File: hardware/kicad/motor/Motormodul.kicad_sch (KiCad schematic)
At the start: 56 parts, among them J100 Stapelstecker links, Pico-Pin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, J101 Kettenstecker, Buchse oben (S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, J102 Kettenstecker, Stift unten (S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, J103 Leistungsstecker, Buchse oben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, J104 Leistungsstecker, Stift unten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, J105 Stapelstecker rechts, Pico-Pi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, J3 Notaus-Ruhestrom, J5 Motor-Klemme, J90 Versorgung Eingang, J95 Randpads GPIO, unbestueckt (T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, J96 Randpads Versorgung: 2x 3V3 +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, Q90 IRFR5305, U1 DRV8876PWPR, U100 STM32C011F6P6, U101 SN74LVC1G175, U102 SN74LVC2G00DCUR, U103 SN74LVC1G08, U3 SN74LVC1G08, U4 PC817, U5 PC817, U6 SN74LVC1G07, U7 SN74LVC1G07, U90 K7805-1000R3

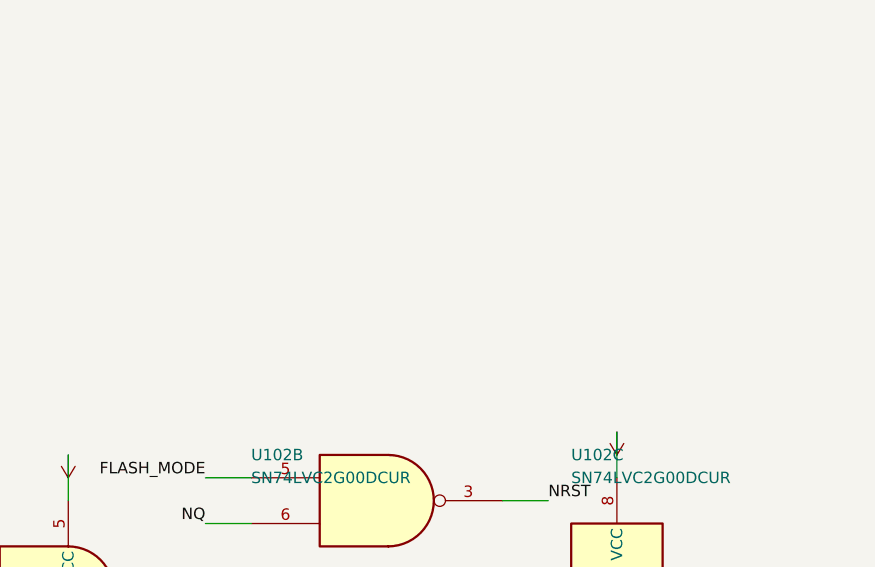
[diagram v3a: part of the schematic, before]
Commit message: Motormodul: fehlende Gatter-Abblockung fuer U101/U102/U103 nachgezogen
Dieselbe Luecke, die Task 6 im Dimmermodul geschlossen hat, bestand im
Motormodul unveraendert: modulsockel.py blockt mit C100 nur die MCU
(U100) ab, C101 ist Teil des NCLR-Loeschglieds -- U101 (SN74LVC1G175),
U102 (SN74LVC2G00DCUR) und U103 (SN74LVC1G08) hatten keinen eigenen
100-nF-Kondensator an ihrer 3V3/GND-Versorgung. Die EIGENEN Gatter des
Motormoduls (U3/U6/U7) waren davon nicht betroffen -- die haben schon
laenger ihre eigenen Abblockkondensatoren C14/C15/C16.

Neue Funktion _gatter_abblockung_sockel() in tools/sch/motormodul.py
setzt C17/C18/C19 (100n/0805, LCSC C49678) an dieselben x/y-Offsets,
die dimmermodul.py fuer C102/C103/C104 verwendet, weil der
Modulsockel-Block in beiden Modulen identischer Code ist. ERC bleibt
bei 0 Fehlern und den zwei vorbestehenden Warnungen
(lib_symbol_mismatch, multiple_net_names). tests/test_motormodul.py
um die drei neuen Refs und eine Gattungspruefung (Pin1->3V3,
Pin2->GND) erweitert.

Co-Authored-By: Claude Fable 5 <noreply@anthropic.com>
Claude-Session: https://claude.ai/code/session_01KDus95JJwCeRuwccgBWEi5
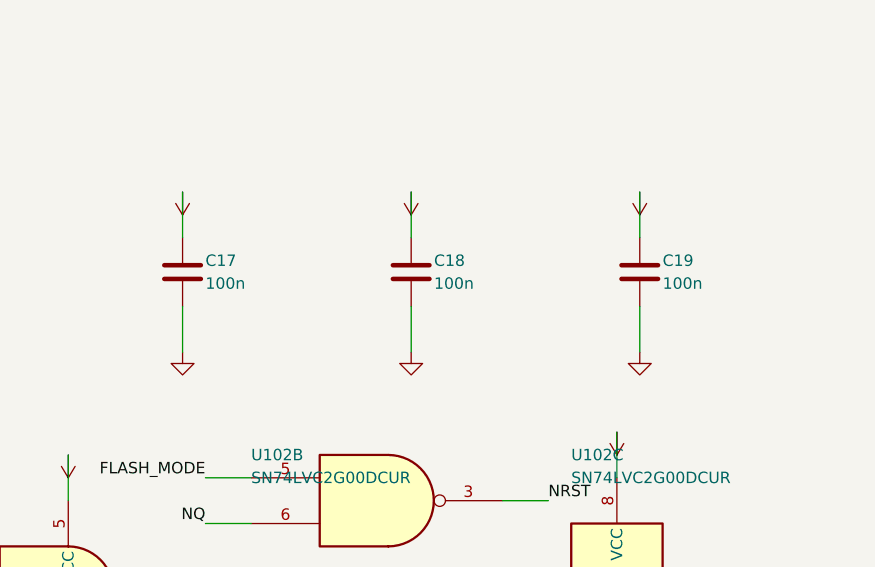
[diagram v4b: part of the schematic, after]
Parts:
- removed C91: 22u, Capacitor_SMD:C_0805_2012Metric_Pad1.18x1.45mm_HandSolder, symbol Device:C
- removed J100: Stapelstecker links, Pico-Pins 1..20 (Buchse), Connector_PinSocket_2.54mm:PinSocket_1x20_P2.54mm_Vertical, symbol Connector_Generic:Conn_01x20
- removed J101: Kettenstecker, Buchse oben (SMD), Connector_PinSocket_2.54mm:PinSocket_1x02_P2.54mm_Vertical_SMD_Pin1Left, symbol Connector_Generic:Conn_01x02
- removed J102: Kettenstecker, Stift unten (SMD), Connector_PinHeader_2.54mm:PinHeader_1x02_P2.54mm_Vertical_SMD_Pin1Left, symbol Connector_Generic:Conn_01x02
- removed J103: Leistungsstecker, Buchse oben (SMD), Connector_PinSocket_2.54mm:PinSocket_2x02_P2.54mm_Vertical_SMD, symbol Connector_Generic:Conn_02x02_Odd_Even
- removed J104: Leistungsstecker, Stift unten (SMD), Connector_PinHeader_2.54mm:PinHeader_2x02_P2.54mm_Vertical_SMD, symbol Connector_Generic:Conn_02x02_Odd_Even
- removed J105: Stapelstecker rechts, Pico-Pins 21..40 (Buchse), Connector_PinSocket_2.54mm:PinSocket_1x20_P2.54mm_Vertical, symbol Connector_Generic:Conn_01x20
- removed U1: DRV8876PWPR, DRV8876PWPR:IC_DRV8876PWPR, symbol DRV8876PWPR:DRV8876PWPR
- removed U90: K7805-1000R3, Converter_DCDC:Converter_DCDC_RECOM_R-78B-2.0_THT, symbol Converter_DCDC:R-78B5.0-2.0
- added C15, C16: 0.1u, Capacitor_SMD:C_0805_2012Metric_Pad1.18x1.45mm_HandSolder, symbol Device:C
- added R100, R101: Kennwiderstand (Modultyp), Resistor_SMD:R_0805_2012Metric_Pad1.20x1.40mm_HandSolder, symbol Device:R
- added R104: 10000 (ID_OBEN), Resistor_SMD:R_0805_2012Metric_Pad1.20x1.40mm_HandSolder, symbol Device:R
- added R17, R19: 3.3k, Resistor_SMD:R_1206_3216Metric, symbol Device:R
- added R20, R21: 4.7k, Resistor_SMD:R_0805_2012Metric_Pad1.20x1.40mm_HandSolder, symbol Device:R
- added U5: PC817, Optocoupler_PC817:PC817_SMT_Gullwing, symbol Isolator:PC817
- added U6, U7: SN74LVC1G07, Package_TO_SOT_SMD:SOT-353_SC-70-5, symbol 74xGxx:74LVC1G07
- C10: renamed from J5; value Motor-Klemme -> 0.022u; footprint TerminalBlock_Phoenix:TerminalBlock_Phoenix_MKDS-3-2-5.08_1x02_P5.08mm_Horizontal -> Capacitor_SMD:C_0805_2012Metric_Pad1.18x1.45mm_HandSolder; symbol Connector:Screw_Terminal_01x02 -> Device:C
- C100: renamed from U102; value SN74LVC2G00DCUR -> 100n; footprint Package_SO:VSSOP-8_2.3x2mm_P0.5mm -> Capacitor_SMD:C_0805_2012Metric_Pad1.18x1.45mm_HandSolder; symbol 74xGxx:74LVC2G00 -> Device:C
- C101: renamed from R100; value Kennwiderstand (Modultyp) -> 1000n; footprint Resistor_SMD:R_0805_2012Metric_Pad1.20x1.40mm_HandSolder -> Capacitor_SMD:C_0805_2012Metric_Pad1.18x1.45mm_HandSolder; symbol Device:R -> Device:C
- C11: renamed from U3; value SN74LVC1G08 -> 0.1u; footprint Package_TO_SOT_SMD:SOT-353_SC-70-5 -> Capacitor_SMD:C_0805_2012Metric_Pad1.18x1.45mm_HandSolder; symbol 74xGxx:74LVC1G08 -> Device:C
- C13: renamed from R20; value 4.7k -> 0.1u; footprint Resistor_SMD:R_0805_2012Metric_Pad1.20x1.40mm_HandSolder -> Capacitor_SMD:C_0805_2012Metric_Pad1.18x1.45mm_HandSolder; symbol Device:R -> Device:C
- C14: renamed from R17; value 3.3k -> 0.1u; footprint Resistor_SMD:R_1206_3216Metric -> Capacitor_SMD:C_0805_2012Metric_Pad1.18x1.45mm_HandSolder; symbol Device:R -> Device:C
- C17: renamed from R91; value 10k -> 100n; footprint Resistor_SMD:R_0805_2012Metric_Pad1.20x1.40mm_HandSolder -> Capacitor_SMD:C_0805_2012Metric_Pad1.18x1.45mm_HandSolder; symbol Device:R -> Device:C; LCSC (none) -> C49678
- C18: renamed from D90; value SMCJ30A -> 100n; footprint Diode_SMD:D_SMC -> Capacitor_SMD:C_0805_2012Metric_Pad1.18x1.45mm_HandSolder; symbol Device:D_Zener -> Device:C; LCSC (none) -> C49678
- C19: renamed from C90; value 220u -> 100n; footprint Capacitor_THT:CP_Radial_D8.0mm_P3.50mm -> Capacitor_SMD:C_0805_2012Metric_Pad1.18x1.45mm_HandSolder; symbol Device:C_Polarized -> Device:C; LCSC (none) -> C49678
- C90: renamed from R8; value 0.1k -> 220u; footprint Resistor_SMD:R_0805_2012Metric_Pad1.20x1.40mm_HandSolder -> Capacitor_THT:CP_Radial_D8.0mm_P3.50mm; symbol Device:R -> Device:C_Polarized
- C91: renamed from R13; value 10k -> 22u; footprint Resistor_SMD:R_0805_2012Metric_Pad1.20x1.40mm_HandSolder -> Capacitor_SMD:C_0805_2012Metric_Pad1.18x1.45mm_HandSolder; symbol Device:R -> Device:C
- D90: renamed from R7; value 0.1k -> SMCJ30A; footprint Resistor_SMD:R_0805_2012Metric_Pad1.20x1.40mm_HandSolder -> Diode_SMD:D_SMC; symbol Device:R -> Device:D_Zener
- D91: renamed from R5; value 1.3k -> SS36C; footprint Resistor_SMD:R_0805_2012Metric_Pad1.20x1.40mm_HandSolder -> Diode_SMD:D_SMC; symbol Device:R -> Device:D_Schottky
- J100: renamed from U100; value STM32C011F6P6 -> Stapelstecker links, Pico-Pins 1..20 (Buchse); footprint Package_SO:TSSOP-20_4.4x6.5mm_P0.65mm -> Connector_PinSocket_2.54mm:PinSocket_1x20_P2.54mm_Vertical; symbol MCU_ST_STM32C0:STM32C011F6Px -> Connector_Generic:Conn_01x20
- J101: renamed from U101; value SN74LVC1G175 -> Kettenstecker, Buchse oben (SMD); footprint Package_TO_SOT_SMD:SOT-363_SC-70-6 -> Connector_PinSocket_2.54mm:PinSocket_1x02_P2.54mm_Vertical_SMD_Pin1Left; symbol 74xGxx:74LVC1G175 -> Connector_Generic:Conn_01x02
- J102: renamed from R102; value 100k -> Kettenstecker, Stift unten (SMD); footprint Resistor_SMD:R_0805_2012Metric_Pad1.20x1.40mm_HandSolder -> Connector_PinHeader_2.54mm:PinHeader_1x02_P2.54mm_Vertical_SMD_Pin1Left; symbol Device:R -> Connector_Generic:Conn_01x02
- J103: renamed from C101; value 1000n -> Leistungsstecker, Buchse oben (SMD); footprint Capacitor_SMD:C_0805_2012Metric_Pad1.18x1.45mm_HandSolder -> Connector_PinSocket_2.54mm:PinSocket_2x02_P2.54mm_Vertical_SMD; symbol Device:C -> Connector_Generic:Conn_02x02_Odd_Even
- J104: renamed from U102; value SN74LVC2G00DCUR -> Leistungsstecker, Stift unten (SMD); footprint Package_SO:VSSOP-8_2.3x2mm_P0.5mm -> Connector_PinHeader_2.54mm:PinHeader_2x02_P2.54mm_Vertical_SMD; symbol 74xGxx:74LVC2G00 -> Connector_Generic:Conn_02x02_Odd_Even
- J105: renamed from C100; value 100n -> Stapelstecker rechts, Pico-Pins 21..40 (Buchse); footprint Capacitor_SMD:C_0805_2012Metric_Pad1.18x1.45mm_HandSolder -> Connector_PinSocket_2.54mm:PinSocket_1x20_P2.54mm_Vertical; symbol Device:C -> Connector_Generic:Conn_01x20
- J3: renamed from U5; value PC817 -> Notaus-Ruhestrom; footprint Optocoupler_PC817:PC817_SMT_Gullwing -> Connector_PinHeader_2.54mm:PinHeader_1x04_P2.54mm_Vertical; symbol Isolator:PC817 -> Connector:Conn_01x04_Pin
- J5: renamed from U6; value SN74LVC1G07 -> Motor-Klemme; footprint Package_TO_SOT_SMD:SOT-353_SC-70-5 -> TerminalBlock_Phoenix:TerminalBlock_Phoenix_MKDS-3-2-5.08_1x02_P5.08mm_Horizontal; symbol 74xGxx:74LVC1G07 -> Connector:Screw_Terminal_01x02; LCSC C7830 -> (none)
- J90: renamed from D91; value SS36C -> Versorgung Eingang; footprint Diode_SMD:D_SMC -> TerminalBlock_Phoenix:TerminalBlock_Phoenix_PT-1,5-2-3.5-H_1x02_P3.50mm_Horizontal; symbol Device:D_Schottky -> Connector:Screw_Terminal_01x02
- J95: renamed from Q90; value IRFR5305 -> Randpads GPIO, unbestueckt (THT-Loetpad); footprint Package_TO_SOT_SMD:TO-252-3_TabPin2 -> Connector_PinHeader_2.54mm:PinHeader_1x18_P2.54mm_Vertical; symbol Transistor_FET:Q_PMOS_GDS -> Connector_Generic:Conn_01x18; now not fitted
- J96: renamed from R90; value 10k -> Randpads Versorgung: 2x 3V3 + 2x GND, unbestueckt (THT-Loetpad); footprint Resistor_SMD:R_0805_2012Metric_Pad1.20x1.40mm_HandSolder -> Connector_PinHeader_2.54mm:PinHeader_1x04_P2.54mm_Vertical; symbol Device:R -> Connector_Generic:Conn_01x04; now not fitted
- Q90: renamed from C9; value 0.1u -> IRFR5305; footprint Capacitor_SMD:C_0805_2012Metric_Pad1.18x1.45mm_HandSolder -> Package_TO_SOT_SMD:TO-252-3_TabPin2; symbol Device:C -> Transistor_FET:Q_PMOS_GDS
- R10: renamed from U4; value PC817 -> 4.7k; footprint Optocoupler_PC817:PC817_SMT_Gullwing -> Resistor_SMD:R_0805_2012Metric_Pad1.20x1.40mm_HandSolder; symbol Isolator:PC817 -> Device:R; now not fitted
- R102: renamed from R104; value 10000 (ID_OBEN) -> 100k
- R105: renamed from J90; value Versorgung Eingang -> 10000 (ID_OBEN); footprint TerminalBlock_Phoenix:TerminalBlock_Phoenix_PT-1,5-2-3.5-H_1x02_P3.50mm_Horizontal -> Resistor_SMD:R_0805_2012Metric_Pad1.20x1.40mm_HandSolder; symbol Connector:Screw_Terminal_01x02 -> Device:R
- R13: renamed from R16; value 3.3k -> 10k; footprint Resistor_SMD:R_1206_3216Metric -> Resistor_SMD:R_0805_2012Metric_Pad1.20x1.40mm_HandSolder
- R15: renamed from R19; value 3.3k -> 10k; footprint Resistor_SMD:R_1206_3216Metric -> Resistor_SMD:R_0805_2012Metric_Pad1.20x1.40mm_HandSolder
- R16: renamed from R21; value 4.7k -> 3.3k; footprint Resistor_SMD:R_0805_2012Metric_Pad1.20x1.40mm_HandSolder -> Resistor_SMD:R_1206_3216Metric
- R18: renamed from U7; value SN74LVC1G07 -> 3.3k; footprint Package_TO_SOT_SMD:SOT-353_SC-70-5 -> Resistor_SMD:R_1206_3216Metric; symbol 74xGxx:74LVC1G07 -> Device:R; LCSC C7830 -> (none)
- R5: renamed from R18; value 3.3k -> 1.3k; footprint Resistor_SMD:R_1206_3216Metric -> Resistor_SMD:R_0805_2012Metric_Pad1.20x1.40mm_HandSolder
- R7: renamed from C14; value 0.1u -> 0.1k; footprint Capacitor_SMD:C_0805_2012Metric_Pad1.18x1.45mm_HandSolder -> Resistor_SMD:R_0805_2012Metric_Pad1.20x1.40mm_HandSolder; symbol Device:C -> Device:R
- R8: renamed from R15; value 10k -> 0.1k
- R9: renamed from J3; value Notaus-Ruhestrom -> 0.1k; footprint Connector_PinHeader_2.54mm:PinHeader_1x04_P2.54mm_Vertical -> Resistor_SMD:R_0805_2012Metric_Pad1.20x1.40mm_HandSolder; symbol Connector:Conn_01x04_Pin -> Device:R
- R90: renamed from C10; value 0.022u -> 10k; footprint Capacitor_SMD:C_0805_2012Metric_Pad1.18x1.45mm_HandSolder -> Resistor_SMD:R_0805_2012Metric_Pad1.20x1.40mm_HandSolder; symbol Device:C -> Device:R
- R91: renamed from C11; value 0.1u -> 10k; footprint Capacitor_SMD:C_0805_2012Metric_Pad1.18x1.45mm_HandSolder -> Resistor_SMD:R_0805_2012Metric_Pad1.20x1.40mm_HandSolder; symbol Device:C -> Device:R
- U1: renamed from R10; value 4.7k -> DRV8876PWPR; footprint Resistor_SMD:R_0805_2012Metric_Pad1.20x1.40mm_HandSolder -> DRV8876PWPR:IC_DRV8876PWPR; symbol Device:R -> DRV8876PWPR:DRV8876PWPR; now fitted
- U100: renamed from U102; value SN74LVC2G00DCUR -> STM32C011F6P6; footprint Package_SO:VSSOP-8_2.3x2mm_P0.5mm -> Package_SO:TSSOP-20_4.4x6.5mm_P0.65mm; symbol 74xGxx:74LVC2G00 -> MCU_ST_STM32C0:STM32C011F6Px
- U101: renamed from U103; value SN74LVC1G08 -> SN74LVC1G175; footprint Package_TO_SOT_SMD:SOT-353_SC-70-5 -> Package_TO_SOT_SMD:SOT-363_SC-70-6; symbol 74xGxx:74LVC1G08 -> 74xGxx:74LVC1G175
- U102: renamed from J95; value Randpads GPIO, unbestueckt (THT-Loetpad) -> SN74LVC2G00DCUR; footprint Connector_PinHeader_2.54mm:PinHeader_1x18_P2.54mm_Vertical -> Package_SO:VSSOP-8_2.3x2mm_P0.5mm; symbol Connector_Generic:Conn_01x18 -> 74xGxx:74LVC2G00; now fitted
- U102: renamed from R105; value 10000 (ID_OBEN) -> SN74LVC2G00DCUR; footprint Resistor_SMD:R_0805_2012Metric_Pad1.20x1.40mm_HandSolder -> Package_SO:VSSOP-8_2.3x2mm_P0.5mm; symbol Device:R -> 74xGxx:74LVC2G00
- U102: renamed from R101; value Kennwiderstand (Modultyp) -> SN74LVC2G00DCUR; footprint Resistor_SMD:R_0805_2012Metric_Pad1.20x1.40mm_HandSolder -> Package_SO:VSSOP-8_2.3x2mm_P0.5mm; symbol Device:R -> 74xGxx:74LVC2G00
- U103: renamed from J96; value Randpads Versorgung: 2x 3V3 + 2x GND, unbestueckt (THT-Loetpad) -> SN74LVC1G08; footprint Connector_PinHeader_2.54mm:PinHeader_1x04_P2.54mm_Vertical -> Package_TO_SOT_SMD:SOT-353_SC-70-5; symbol Connector_Generic:Conn_01x04 -> 74xGxx:74LVC1G08; now fitted
- U3: renamed from C15; value 0.1u -> SN74LVC1G08; footprint Capacitor_SMD:C_0805_2012Metric_Pad1.18x1.45mm_HandSolder -> Package_TO_SOT_SMD:SOT-353_SC-70-5; symbol Device:C -> 74xGxx:74LVC1G08
- U4: renamed from C16; value 0.1u -> PC817; footprint Capacitor_SMD:C_0805_2012Metric_Pad1.18x1.45mm_HandSolder -> Optocoupler_PC817:PC817_SMT_Gullwing; symbol Device:C -> Isolator:PC817
- U90: renamed from R9; value 0.1k -> K7805-1000R3; footprint Resistor_SMD:R_0805_2012Metric_Pad1.20x1.40mm_HandSolder -> Converter_DCDC:Converter_DCDC_RECOM_R-78B-2.0_THT; symbol Device:R -> Converter_DCDC:R-78B5.0-2.0
- renumbered C13 to C9
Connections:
- net +24V: now also C11.2, C9.1, C90.1, D90.1 (K), J103.1 (Pin_1), J103.3 (Pin_3), J104.1 (Pin_1), J104.3 (Pin_3), Q90.3 (S), R16.1, R90.2, U1.11 (VM), U90.1 (IN), R17.1; no longer C14.1, C18.1 (K), C19.1, J95.3 (S), J96.2, Q90.1, R13.1, R91.2
- net +5V_LOKAL: now also C91.1, D91.2 (A), U90.3 (OUT); no longer J90.2 (A)
- net 3V3: now also C100.1, C100.2, C11.1, C14.1, C14.2, C17.1, C18.1, C19.1, C90.2, C91.2, D90.2 (A), J100.13 (Pin_13), J100.18 (Pin_18), J100.3 (Pin_3), J100.8 (Pin_8), J102.2 (Pin_2), J103.4 (Pin_4), J104.2 (Pin_2), J104.4 (Pin_4), J105.13 (Pin_13), J105.16 (Pin_16), J105.18 (Pin_18), J105.3 (Pin_3), J105.8 (Pin_8), J90.2 (Pin_2), J96.1 (Pin_1), J96.2 (Pin_2), J96.3 (Pin_3), J96.4 (Pin_4), R105.1, R13.1, R15.1, R5.2, R91.2, U1.15 (GND), U1.16 (PMODE), U1.17 (EXP), U1.5 (VREF), U1.7 (IMODE), U1.9 (PGND), U100.4 (VDD), U100.5 (VSS), U101.2 (GND), U102.4 (GND), U102.8 (VCC), U103.5 (VCC), U3.3 (GND), U3.5 (VCC), U4.4, U90.2 (GND), C15.1, C15.2, C16.1, C16.2, R100.2, R101.2, R104.1, R20.2, R21.2, U5.2, U5.4, U6.3 (GND), U6.5 (VCC), U7.3 (GND), U7.5 (VCC); no longer C100.4 (GND), C100.8 (VCC), C11.3 (GND), C11.5 (VCC), C9.2, C91.1, D91.2, J100.4 (VDD), J100.5 (VSS), J101.5 (VCC), J102.1, J105.1, J105.2, J3.2, J3.4, J5.3 (GND), J5.5 (VCC), R10.4, R105.2 (Pin_2), R16.2, R18.3 (GND), R18.5 (VCC), R7.1, R7.2, R8.1, R91.1, U1.2, U101.3 (GND), U102.1, U102.2, U103.1 (Pin_1), U103.2 (Pin_2), U103.4 (Pin_4), U3.1, U3.2, U4.1
- net BOOT0: now also U100.19 (PA14), U103.4; no longer J100.19 (PA14), U101.4
- net CPH: now also C10.1, U1.13 (CPH); no longer R90.1
- net CPL: now also C10.2, U1.14 (CPL); no longer R90.2
- net FLASH_MODE: now also J100.5 (Pin_5), U102.5, U103.1; no longer U100.5, U101.1
- net FLASH_RX: now also J100.2 (Pin_2), U100.16 (PA9/PA11); no longer J100.16 (PA9/PA11)
- net FLASH_TX: now also J100.1 (Pin_1), U100.17 (PA10/PA12); no longer J100.17 (PA10/PA12)
- net GP10: now also J100.14 (Pin_14), J95.3 (Pin_3); no longer U102.3 (Pin_3)
- net GP11: now also J100.15 (Pin_15), J95.4 (Pin_4); no longer U102.4 (Pin_4)
- net GP12: now also J100.16 (Pin_16), J95.5 (Pin_5); no longer U102.5 (Pin_5)
- net GP13: now also J100.17 (Pin_17), J95.6 (Pin_6); no longer U102.6 (Pin_6)
- net GP14: now also J100.19 (Pin_19), J95.7 (Pin_7); no longer U102.7 (Pin_7)
- net GP15: now also J100.20 (Pin_20), J95.8 (Pin_8); no longer U102.8 (Pin_8)
- net GP16: now also J105.1 (Pin_1), J95.9 (Pin_9); no longer U102.9 (Pin_9)
- net GP17: now also J105.2 (Pin_2), J95.10 (Pin_10); no longer U102.10 (Pin_10)
- net GP18: now also J105.4 (Pin_4), J95.11 (Pin_11); no longer U102.11 (Pin_11)
- net GP19: now also J105.5 (Pin_5), J95.12 (Pin_12); no longer U102.12 (Pin_12)
- net GP20: now also J105.6 (Pin_6), J95.13 (Pin_13); no longer U102.13 (Pin_13)
- net GP21: now also J105.7 (Pin_7), J95.14 (Pin_14); no longer U102.14 (Pin_14)
- net GP22: now also J105.9 (Pin_9), J95.15 (Pin_15); no longer U102.15 (Pin_15)
- net GP26: now also J105.11 (Pin_11), J95.16 (Pin_16); no longer U102.16 (Pin_16)
- net GP27: now also J105.12 (Pin_12), J95.17 (Pin_17); no longer U102.17 (Pin_17)
- net GP28: now also J105.14 (Pin_14), J95.18 (Pin_18); no longer U102.18 (Pin_18)
- net GP8: now also J100.11 (Pin_11), J95.1 (Pin_1); no longer U102.1 (Pin_1)
- net GP9: now also J100.12 (Pin_12), J95.2 (Pin_2); no longer U102.2 (Pin_2)
- net I2C_SCL: now also J100.7 (Pin_7), U100.20 (PB6); no longer J100.20 (PB6)
- net I2C_SDA: now also J100.6 (Pin_6), U100.1 (PB7); no longer J100.1 (PB7)
- net ID0: now also U100.7 (PA0), R100.1, R104.2; no longer C101.1, J100.7 (PA0), R102.2
- net ID1: now also R105.2, U100.8 (PA1), R101.1; no longer J100.8 (PA1), U102.1, U102.2
- net IN1: now also R7.1, U100.9 (PA2); no longer D90.1, J100.9 (PA2)
- net IN2: now also R8.1, U100.10 (PA3); no longer C90.1, J100.10 (PA3)
- net IPROPI: now also C13.1, R10.1, R5.1, U1.6 (IPROPI), U100.13 (PA6); no longer C9.1, D91.1, J100.13 (PA6), U1.1
- net KREIS1_A: now also J3.1 (Pin_1), R16.2; no longer R13.2, R9.1 (Pin_1)
- net KREIS1_B: now also J3.2 (Pin_2), R18.1; no longer R5.1, R9.2 (Pin_2)
- net KREIS2_A: now also J3.3 (Pin_3), R17.2; no longer C14.2, R9.3 (Pin_3)
- net KREIS2_B: now also J3.4 (Pin_4), R19.1; no longer R15.1, R9.4 (Pin_4)
- net NCLR: now also C101.1, R102.2, U101.6 (~{CLR}); no longer J101.6 (~{CLR}), J102.2, J103.1
- net NFAULT: now also R13.2, U1.4 (~{NFAULT}), U100.12 (PA5); no longer C91.2, J100.12 (PA5)
- net NOTAUS: now also J100.9 (Pin_9), R15.2, U3.2, U6.4, U7.4; no longer C11.2, J5.4, R18.4, R8.2
- net NQ: now also U102.6, U102.7; no longer J104.7, U100.6
- net NRST: now also U100.6 (PF2), U102.3; no longer J100.6 (PF2), U100.3
- net NSLEEP: now also R9.1, U100.11 (PA4); no longer J100.11 (PA4), U90.1
- net NSLEEP_GATTER: now also R9.2, U3.1; no longer C11.1, U90.2
- net Out1: now also J5.1 (Pin_1), U1.8 (OUT1); no longer C10.1 (Pin_1)
- net Out2: now also J5.2 (Pin_2), U1.10 (OUT2); no longer C10.2 (Pin_2)
- net PWR_IN: now also J90.1 (Pin_1), Q90.2 (D); no longer J95.2 (D), R105.1 (Pin_1)
- net Q90_GATE: now also Q90.1 (G), R90.1, R91.1; no longer C17.1, J95.1 (G), J96.1
- net SCHLEIFE_1: now also U100.3 (PC15), U4.3, R20.1, U6.2; no longer C13.1, J100.3 (PC15), J5.2, R10.3
- net SCHLEIFE_2: now also U100.14 (PA7), R21.1, U5.3, U7.2; no longer J100.14 (PA7), J3.3, R16.1, R18.2
- net SEL_CLK: now also J100.10 (Pin_10), U101.1 (C); no longer J101.1 (C)
- net SEL_IN: now also J101.1 (Pin_1), U101.3 (D); no longer J101.3 (D)
- net SEL_OUT: now also J102.1 (Pin_1), U101.4 (Q), U102.1, U102.2, U103.2; no longer J101.4 (Q), J104.1, J104.2, U101.2
- net U1_EN_IN1: now also R7.2, U1.1 (EN/IN1); no longer D90.2
- net U1_NSLEEP: now also U1.3 (NSLEEP), U3.4; no longer C11.4
- net U1_PH_IN2: now also R8.2, U1.2 (PH/IN2); no longer C90.2
- net U4_LED_A: now also R18.2, U4.1; no longer R10.1, R5.2
- net U5_LED_A: now also R19.2, U5.1; no longer J3.1, R15.2
- net VCP: now also C9.2, U1.12 (VCP); no longer Q90.2
- net VSYS: now also D91.1 (K), J105.19 (Pin_19); no longer J90.1 (K)
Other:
- moved on the sheet: C9, J100, R102, R13, R15, R16, R5, R8, U103

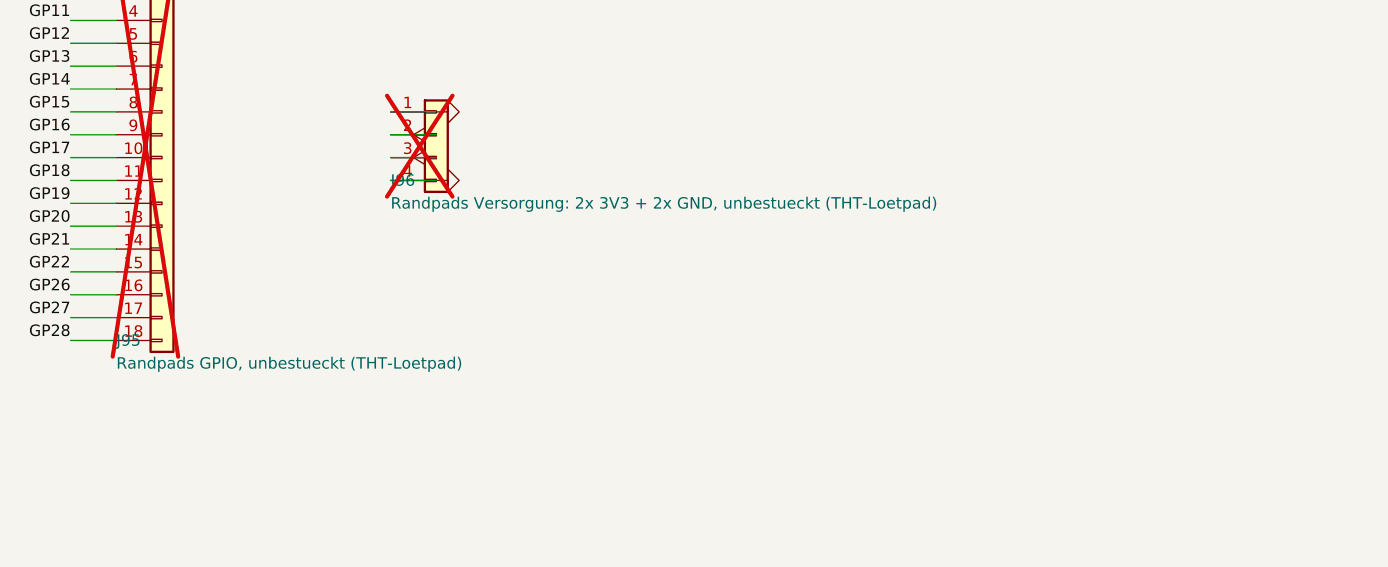
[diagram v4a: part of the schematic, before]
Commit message: Fix-Runde 2 zu Aufgabe 7: Randpads auf B.Cu, Verdreh-Kupferregel erfuellt
Steckerprobe jetzt VOLLSTAENDIG gruen, einschliesslich
"Verdreht 46 Landepunkte, alle >= 1.5 mm von freiliegendem Kupfer" --
ohne jede Ausnahmeliste, wie im Ruling verlangt.

RANDPADS AUF DIE RUECKSEITE (Ruling). Auf der Oberseite ist die Klausel
mit einer 2,54-mm-Padreihe unerfuellbar: auf dem Raster liegt immer ein
Pad <= 1,27 mm von jedem x, minus 0,85 mm Padhalbbreite bleiben 0,42 --
verlangt sind 1,5. Sechs der 22 VERTRAGLICHEN Randpad-Koordinaten
brachen die Regel selbst, drei davon mit Abstand 0,000 mm. Auf B.Cu
bleibt die Schutzzusage voll erhalten (ein verdreht gestecktes Modul
trifft nur F.Cu), und es bleiben Loetpads.

Dafuer zwei projekteigene Footprints (hardware/kicad/components/
footprints/Randpads.pretty): Loetpads in EINER Reihe genau auf dem
Raster. Die Bibliotheks-Stiftleisten gehen beide nicht -- die bedrahtete
legt zwangslaeufig Kupfer auf F.Cu, die SMD-Variante versetzt ihre Pads
abwechselnd um +-1,655 mm und wuerde die 22 Vertragskoordinaten brechen.
Pads bewusst in NEGATIVER x-Richtung angelegt, weil der Footprint immer
gespiegelt eingebaut wird; erst die Spiegelung dreht die Reihe in die
Leserichtung der Labels. Padbreite 0,90 mm ist nach oben begrenzt: der
M3-Freihaltebereich des Ecklochs (4|61) reicht bis x = 7,5, das erste
Randpad sitzt laut Vertrag bei 8,0 -- breiteres Kupfer laege unter dem
Abstandsbolzen. (Die Vertrags-Herleitung von RAND_X0 rechnet nur mit dem
Pad-MITTELPUNKT; s. Bericht.) RAND_Y = 63,0 gilt jetzt unveraendert --
die alte 0,27-mm-Abweichung war eine Folge des Stiftleisten-Hofes.

KLASSE A, aber anders als bestellt. U1 und J5 wandern 0,50 mm nach
Westen -- STARR mitsamt C9/C10/C11 und der ganzen Vorverdrahtung
(_MOTOR_DX), damit alle Abstaende INNERHALB der Motorstufe unveraendert
gueltig bleiben. Das Nest liess sich dagegen NICHT verschieben: es
klemmt zwischen zwei Landezonen (x = 26,61, Spiegel von stapel_rechts,
und x = 12,50/9,96 bei y = 16,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
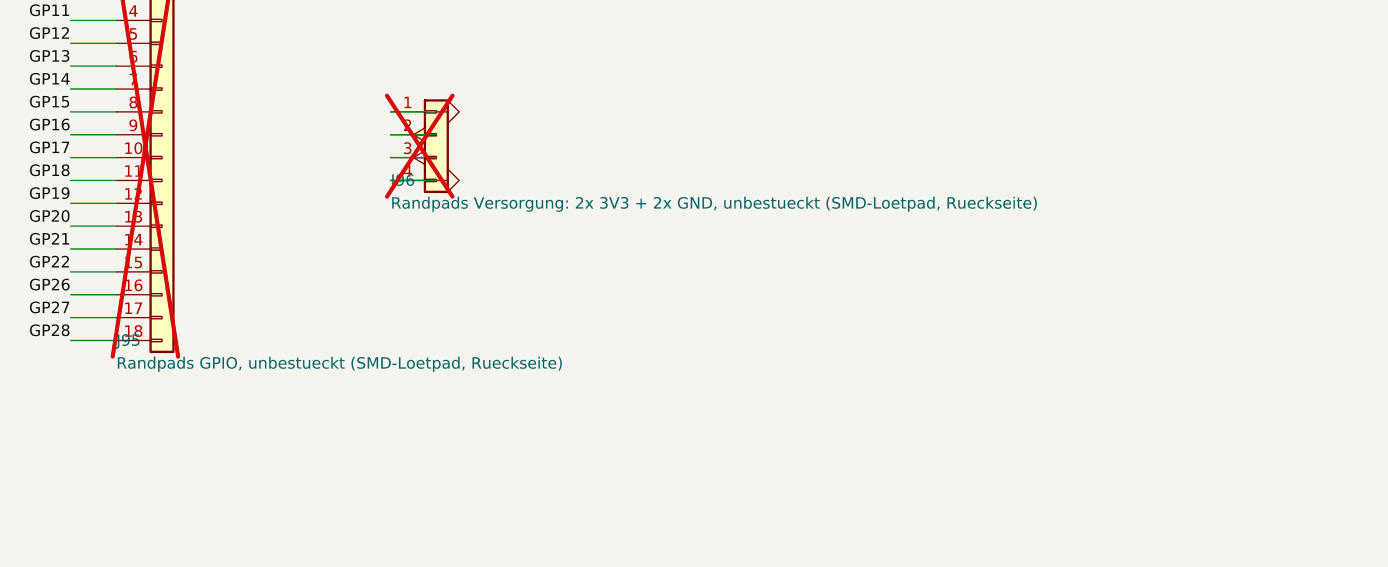
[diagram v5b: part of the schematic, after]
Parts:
- J95: value Randpads GPIO, unbestueckt (THT-Loetpad) -> Randpads GPIO, unbestueckt (SMD-Loetpad, Rueckseite); footprint Connector_PinHeader_2.54mm:PinHeader_1x18_P2.54mm_Vertical -> Randpads:Randpad_Reihe_1x18
- J96: value Randpads Versorgung: 2x 3V3 + 2x GND, unbestueckt (THT-Loetpad) -> Randpads Versorgung: 2x 3V3 + 2x GND, unbestueckt (SMD-Loetpad, Rueckseite); footprint Connector_PinHeader_2.54mm:PinHeader_1x04_P2.54mm_Vertical -> Randpads:Randpad_Reihe_1x04
